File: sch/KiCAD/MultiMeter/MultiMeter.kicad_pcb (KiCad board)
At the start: 2 copper layers, 35.6 x 58.5 mm, 24 parts, among them J1 Conn_01x02_Male, J2 Conn_01x02_Male, J3 Conn_01x03_Male, J4 Conn_01x03_Male, J5 Conn_01x03_Female, J6 Conn_01x15, J7 Conn_01x15, J8 Conn_01x08_Female, J9 Conn_01x02_Female, Q1 2SC1815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

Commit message: 回路図更新
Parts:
- added J10: Conn_01x04_Female, Connector_Molex:Molex_SPOX_5268-04A_1x04_P2.50mm_Horizontal, F.Cu at (40.6, 67.6)
- J8: footprint Connector_JST:JST_XH_B8B-XH-A_1x08_P2.50mm_Vertical -> Connector_JST:JST_XH_S8B-XH-A-1_1x08_P2.50mm_Horizontal
- moved J8 17.1 mm to (57.4, 17.5), turned to 180 degrees
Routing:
- net Net-(A1-Pad1): track 3.18 -> 52.0 mm
- net Net-(A1-Pad2): track 3.18 -> 48.9 mm
- net GNDPWR: track 136.8 -> 142.8 mm
- net +5V: track 101.0 -> 105.3 mm
- net Net-(A1-Pad24): track 32.4 -> 29.5 mm
- net Net-(A1-Pad23): track 50.5 -> 48.2 mm
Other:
- board size 35.6 x 58.5 mm -> 36.1 x 60.3 mm
- board text added: "2023/11/17"
- board text removed: "2023/07/01"

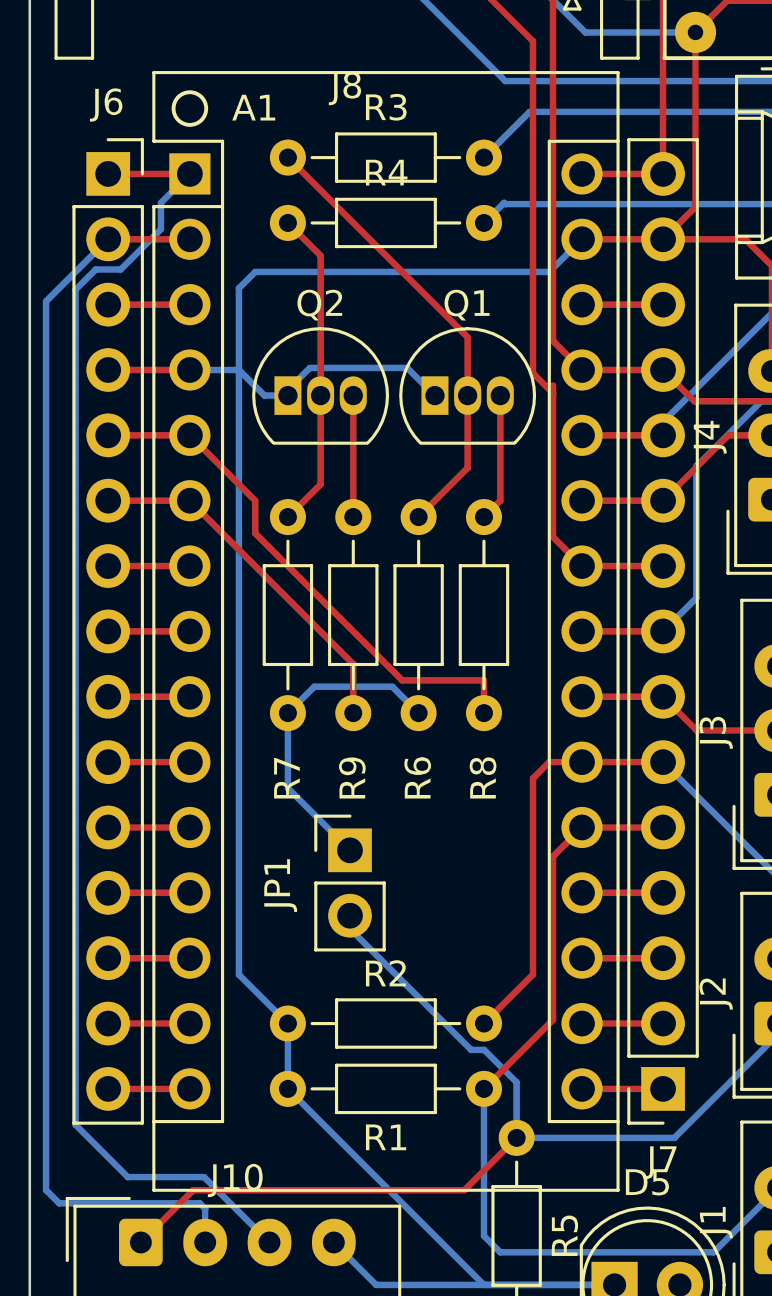
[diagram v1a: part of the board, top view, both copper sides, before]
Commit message: 回路図、パターンを修正
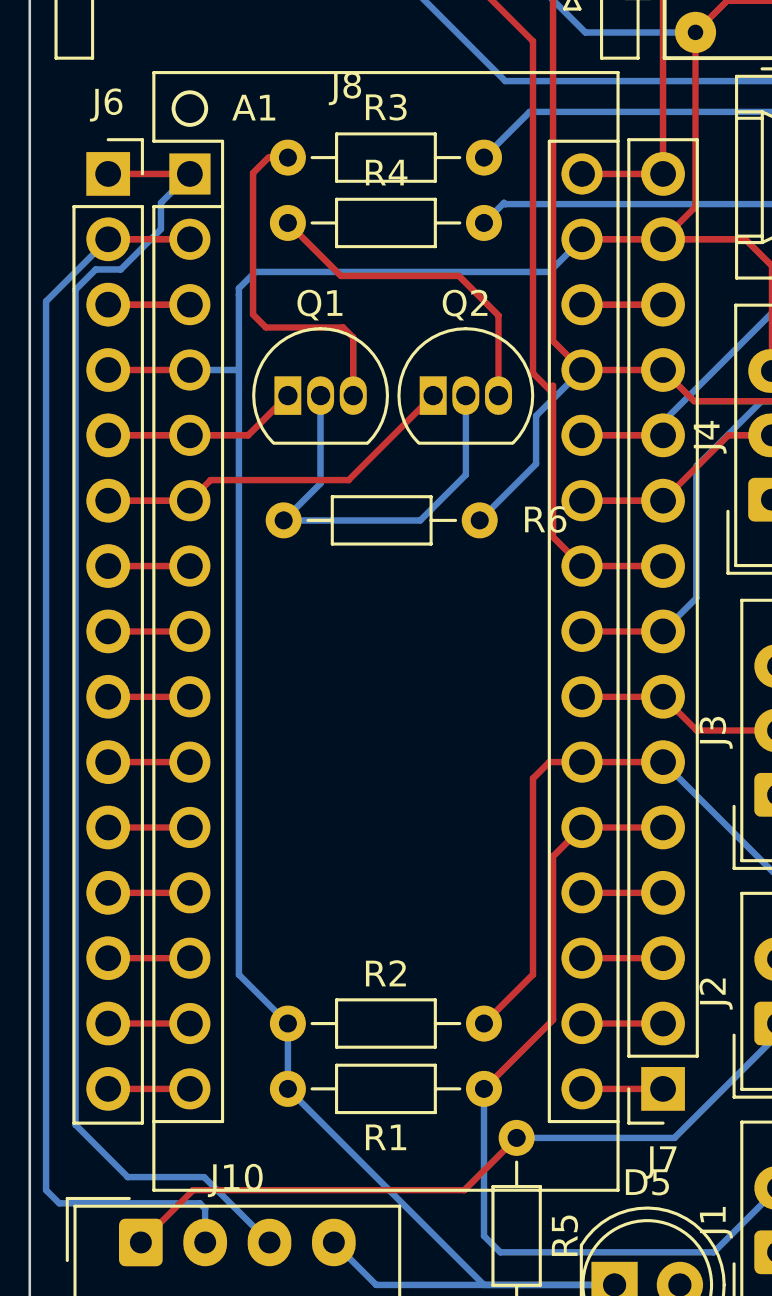
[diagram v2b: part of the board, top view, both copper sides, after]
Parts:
- removed JP1: Jumper_2_Open, Connector_PinHeader_2.54mm:PinHeader_1x02_P2.54mm_Vertical
- removed R7, R8, R9: 10K ohm, Resistor_THT:R_Axial_DIN0204_L3.6mm_D1.6mm_P7.62mm_Horizontal
- moved Q1 5.72 mm to (46.4, 34.6)
- moved Q2 5.65 mm to (52.0, 34.6)
- moved R6 5.25 mm to (46.2, 39.5), turned to 0 degrees
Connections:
- A1 pad 5: Net-(A1-Pad5) -> Net-(A1-D2)
- A1 pad 6: Net-(A1-Pad6) -> Net-(A1-D3)
- J6 pad 5: Net-(A1-Pad5) -> Net-(A1-D2)
- J6 pad 6: Net-(A1-Pad6) -> Net-(A1-D3)
- Q1 pad 1: GNDPWR -> Net-(A1-D2)
- Q1 pad 2: Net-(Q1-Pad2) -> Net-(Q1-C)
- Q1 pad 3: Net-(Q1-Pad3) -> Net-(Q1-B)
- Q2 pad 1: GNDPWR -> Net-(A1-D3)
- Q2 pad 2: Net-(Q2-Pad2) -> Net-(Q1-C)
- Q2 pad 3: GNDPWR -> Net-(Q2-B)
- R3 pad 1: Net-(Q1-Pad2) -> Net-(Q1-B)
- R4 pad 1: Net-(Q2-Pad2) -> Net-(Q2-B)
- R6 pad 1: Net-(Q1-Pad2) -> Net-(Q1-C)
- R6 pad 2: Net-(JP1-Pad1) -> +5V
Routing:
- net Net-(A1-Pad5): track 20.6 -> 0.00 mm
- net Net-(Q1-Pad2): track 17.7 -> 0.00 mm
- net Net-(Q1-C): track 0.00 -> 16.8 mm
- net Net-(A1-D3): track 0.00 -> 14.3 mm
- net Net-(A1-Pad6): track 14.1 -> 0.00 mm
- net GNDPWR: track 142.8 -> 129.0 mm
- net Net-(Q1-B): track 0.00 -> 13.6 mm
- net Net-(Q2-B): track 0.00 -> 12.8 mm
- net Net-(Q2-Pad2): track 12.5 -> 0.00 mm
- net Net-(JP1-Pad1): track 12.3 -> 0.00 mm
- net Net-(A1-D2): track 0.00 -> 7.85 mm
- net Net-(Q1-Pad3): track 4.98 -> 0.00 mm
- net +5V: track 105.3 -> 101.2 mm

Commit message: 回路図修正中
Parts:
- added A2: Arduino_Nano_v3.x, Module:Arduino_Nano, F.Cu at (43.9, 31.9)
- added J11: Conn_01x08_Female, Connector_JST:JST_XH_S8B-XH-A-1_1x08_P2.50mm_Horizontal, F.Cu at (60.3, 23.2)
- added J12: Conn_01x04_Female, Connector_Molex:Molex_SPOX_5268-04A_1x04_P2.50mm_Horizontal, F.Cu at (45.0, 73.5)
- added J13: Conn_01x15, Connector_PinSocket_2.54mm:PinSocket_1x15_P2.54mm_Vertical, F.Cu at (40.0, 31.9)
- added J14: Conn_01x03_Pin, Connector_PinHeader_2.54mm:PinHeader_1x03_P2.54mm_Vertical, F.Cu at (36.6, 37.2)
- added SW1: SW_Push, Button_Switch_THT:SW_PUSH_6mm, F.Cu at (26.5, 29.7)
- added SW2: SW_Push, Button_Switch_THT:SW_PUSH_6mm, F.Cu at (26.5, 38.2)
- added SW3: SW_Push, Button_Switch_THT:SW_PUSH_6mm, F.Cu at (26.5, 46.8)
- moved J6 31.1 mm to (69.9, 32.0)
- moved Q1 31.1 mm to (76.9, 40.6)
- moved R3 31.1 mm to (76.9, 31.4)
- moved R4 31.1 mm to (76.9, 33.9)
- moved R5 31.1 mm to (85.8, 77.1)
- moved A1 31.1 mm to (73.1, 32.0)
- moved D5 31.1 mm to (89.6, 75.2)
- moved J1 31.1 mm to (95.9, 73.9)
- moved J10 31.1 mm to (71.2, 73.5)
- moved J2 31.1 mm to (95.9, 65.0)
- moved J3 31.1 mm to (95.9, 56.1)
- moved J4 31.1 mm to (95.7, 44.7)
- moved J5 31.1 mm to (97.3, 29.6)
- moved J7 31.1 mm to (91.5, 67.6)
- moved J9 31.1 mm to (99.6, 22.7)
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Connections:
- A1 pad 29: GNDPWR -> +5V
- A1 pad 4: GNDPWR -> +5V
- D5 pad 1: GNDPWR -> +5V
- J10 pad 4: GNDPWR -> +5V
- J3 pad 3: GNDPWR -> +5V
- J4 pad 3: GNDPWR -> +5V
- J6 pad 4: GNDPWR -> +5V
- J7 pad 14: GNDPWR -> +5V
- J8 pad 2: GNDPWR -> +5V
- J9 pad 2: GNDPWR -> +5V
- R1 pad 2: GNDPWR -> +5V
- R2 pad 2: GNDPWR -> +5V
- RV1 pad 2: GNDPWR -> +5V
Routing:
- net +5V: track 101.2 -> 400.2 mm
- net GNDPWR: track 129.0 -> 0.00 mm
- net +3.3V: track 0.00 -> 66.8 mm
- net Net-(A2-D1/TX): track 0.00 -> 57.0 mm
- net Net-(A2-D0/RX): track 0.00 -> 50.0 mm
- net Net-(A2-A4): track 0.00 -> 39.0 mm
- net Net-(A2-A5): track 0.00 -> 32.7 mm
- net Net-(J14-Pin_3): track 0.00 -> 16.9 mm
- net Net-(J14-Pin_1): track 0.00 -> 11.4 mm
- net Net-(J14-Pin_2): track 0.00 -> 11.3 mm
- net Net-(J13-Pin_3): track 0.00 -> 3.90 mm
- net Net-(A2-D9): track 0.00 -> 3.90 mm
- net Net-(A2-D8): track 0.00 -> 3.90 mm
- net Net-(A2-D7): track 0.00 -> 3.90 mm
- net Net-(A2-D5): track 0.00 -> 3.90 mm
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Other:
- board size 36.1 x 60.3 mm -> 78.6 x 60.3 mm

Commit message: 回路図、基板を修正
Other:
- outline, holes or cut-outs redrawn
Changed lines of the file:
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@@
 	)
 	(gr_rect
-		(start 24.35898 20.311)
+		(start 66.35898 20.311)
 		(end 102.92698 80.636)
 		(stroke
@@
 		)
 		(fill none)
+		(layer "Edge.Cuts")
+	)
+	(gr_rect
+		(start 24.33358 20.311)
+		(end 63.85898 80.6)
+		(stroke
+			(width 0.1)
+			(type default)
+		)
+		(fill none)

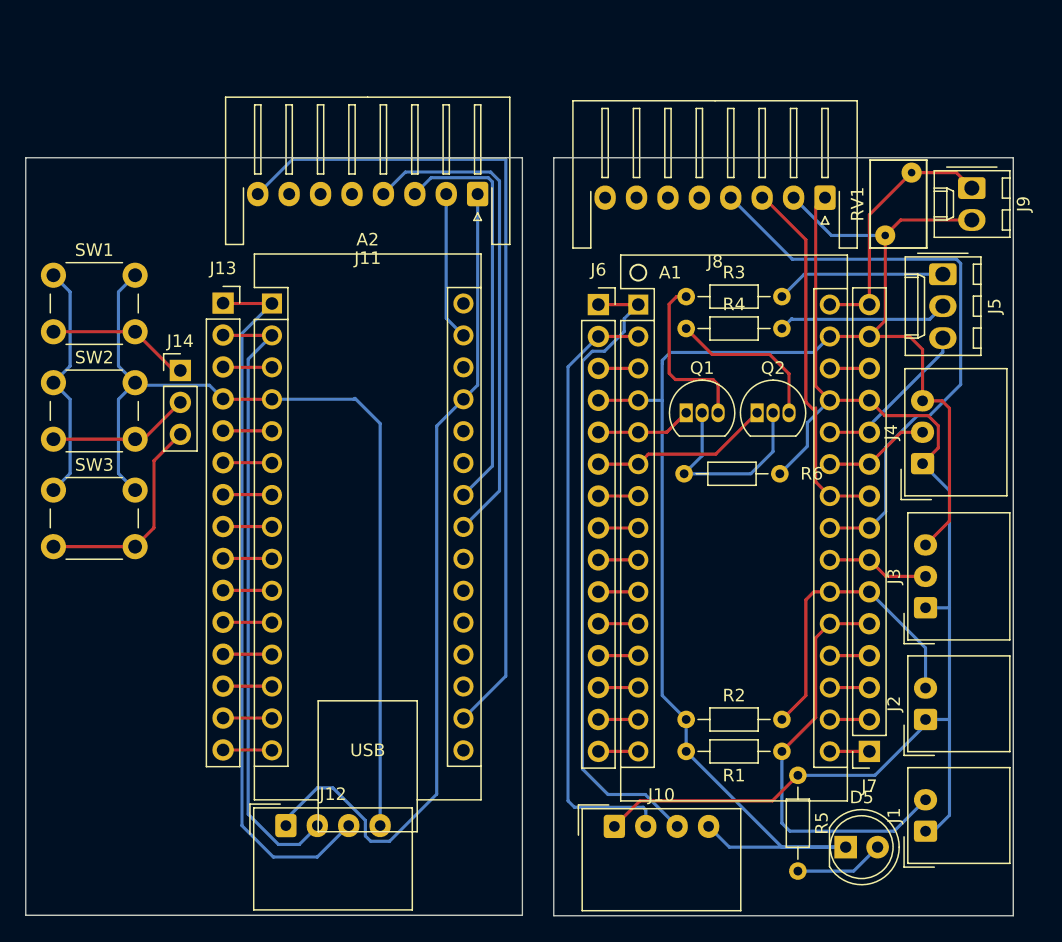
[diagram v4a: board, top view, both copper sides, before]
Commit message: 複製した回路図の重複部分を削除
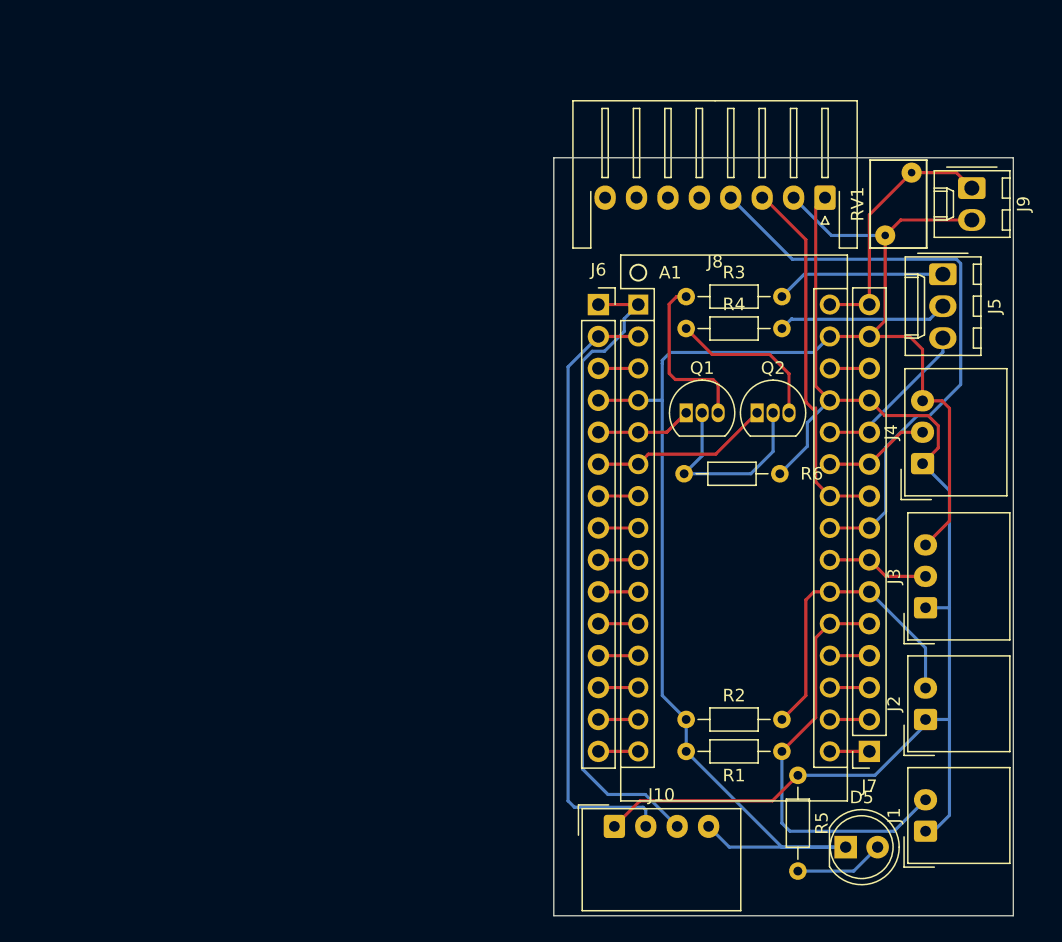
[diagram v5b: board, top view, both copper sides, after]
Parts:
- removed A2: Arduino_Nano_v3.x, Module:Arduino_Nano
- removed J11: Conn_01x08_Female, Connector_JST:JST_XH_S8B-XH-A-1_1x08_P2.50mm_Horizontal
- removed J12: Conn_01x04_Female, Connector_Molex:Molex_SPOX_5268-04A_1x04_P2.50mm_Horizontal
- removed J13: Conn_01x15, Connector_PinSocket_2.54mm:PinSocket_1x15_P2.54mm_Vertical
- removed J14: Conn_01x03_Pin, Connector_PinHeader_2.54mm:PinHeader_1x03_P2.54mm_Vertical
- removed SW1, SW2, SW3: SW_Push, Button_Switch_THT:SW_PUSH_6mm
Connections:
- A1 pad 29: +5V -> GNDPWR
- A1 pad 4: +5V -> GNDPWR
- D5 pad 1: +5V -> GNDPWR
- J10 pad 4: +5V -> GNDPWR
- J3 pad 3: +5V -> GNDPWR
- J4 pad 3: +5V -> GNDPWR
- J6 pad 4: +5V -> GNDPWR
- J7 pad 14: +5V -> GNDPWR
- J8 pad 2: +5V -> GNDPWR
- J9 pad 2: +5V -> GNDPWR
- R1 pad 2: +5V -> GNDPWR
- R2 pad 2: +5V -> GNDPWR
- RV1 pad 2: +5V -> GNDPWR
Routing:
- net +5V: track 400.2 -> 101.2 mm
- net GNDPWR: track 0.00 -> 129.0 mm
- net +3.3V: track 66.8 -> 0.00 mm
- net Net-(A2-D1/TX): track 57.0 -> 0.00 mm
- net Net-(A2-D0/RX): track 50.0 -> 0.00 mm
- net Net-(A2-A4): track 39.0 -> 0.00 mm
- net Net-(A2-A5): track 32.7 -> 0.00 mm
- net Net-(J14-Pin_3): track 16.9 -> 0.00 mm
- net Net-(J14-Pin_1): track 11.4 -> 0.00 mm
- net Net-(J14-Pin_2): track 11.3 -> 0.00 mm
- net Net-(J13-Pin_3): track 3.90 -> 0.00 mm
- net Net-(A2-D9): track 3.90 -> 0.00 mm
- net Net-(A2-D8): track 3.90 -> 0.00 mm
- net Net-(A2-D7): track 3.90 -> 0.00 mm
- net Net-(A2-D5): track 3.90 -> 0.00 mm
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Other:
- board size 78.6 x 60.3 mm -> 36.6 x 60.3 mm
